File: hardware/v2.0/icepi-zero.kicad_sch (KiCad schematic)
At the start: 29 parts, among them J1 Conn_02x20_Counter_Clockwise, SW1 SW_Push, SW2 SW_Push, U1 ECP5U-25F-CABGA256, Y1 SG-8018CG 50.000000MHz

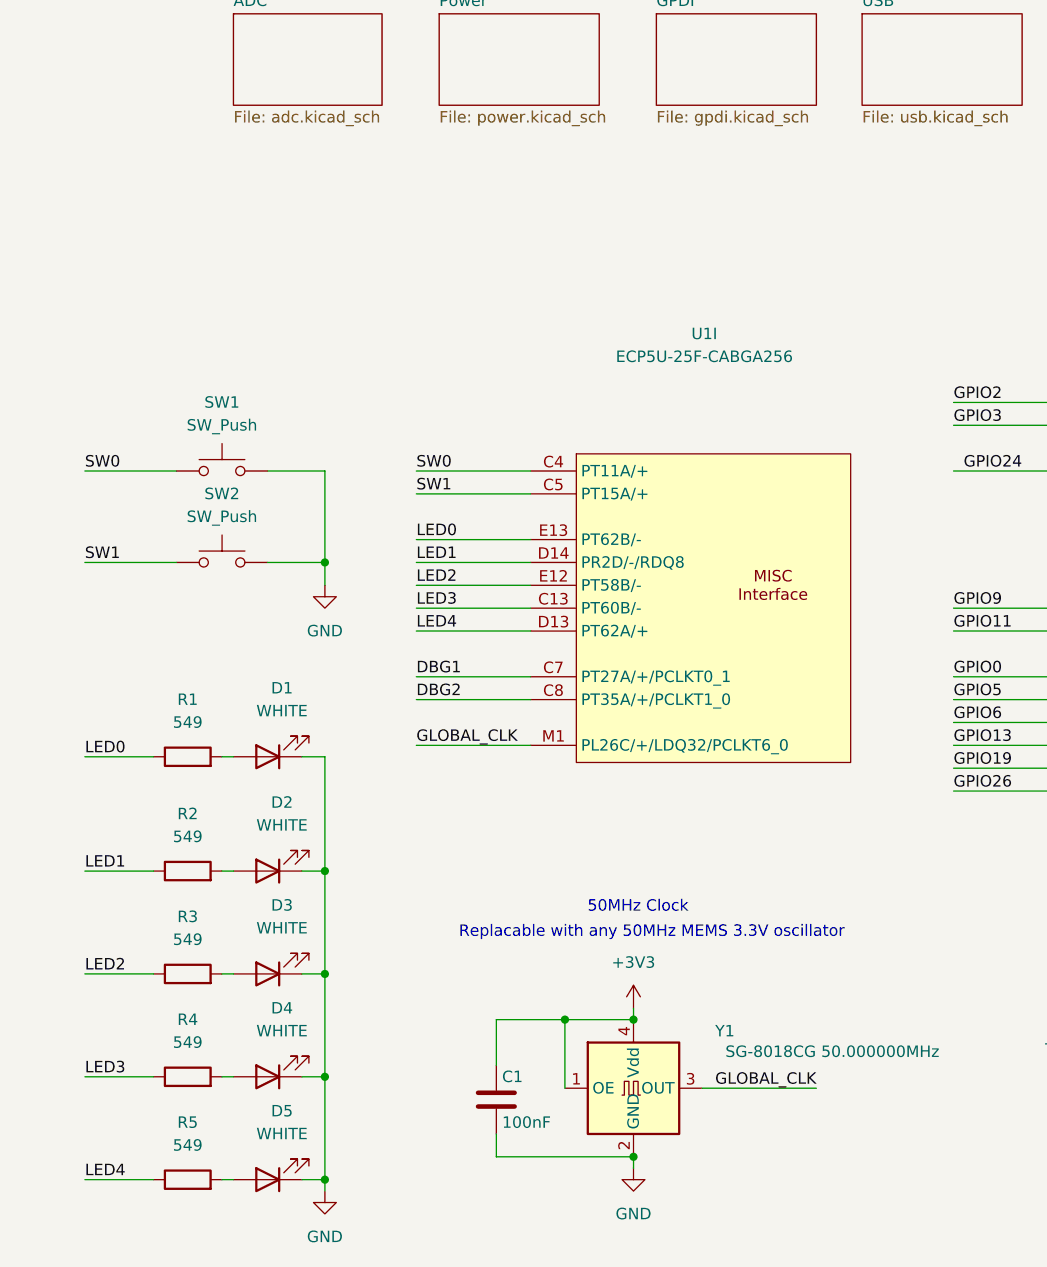
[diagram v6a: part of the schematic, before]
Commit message: LEDs update for IC
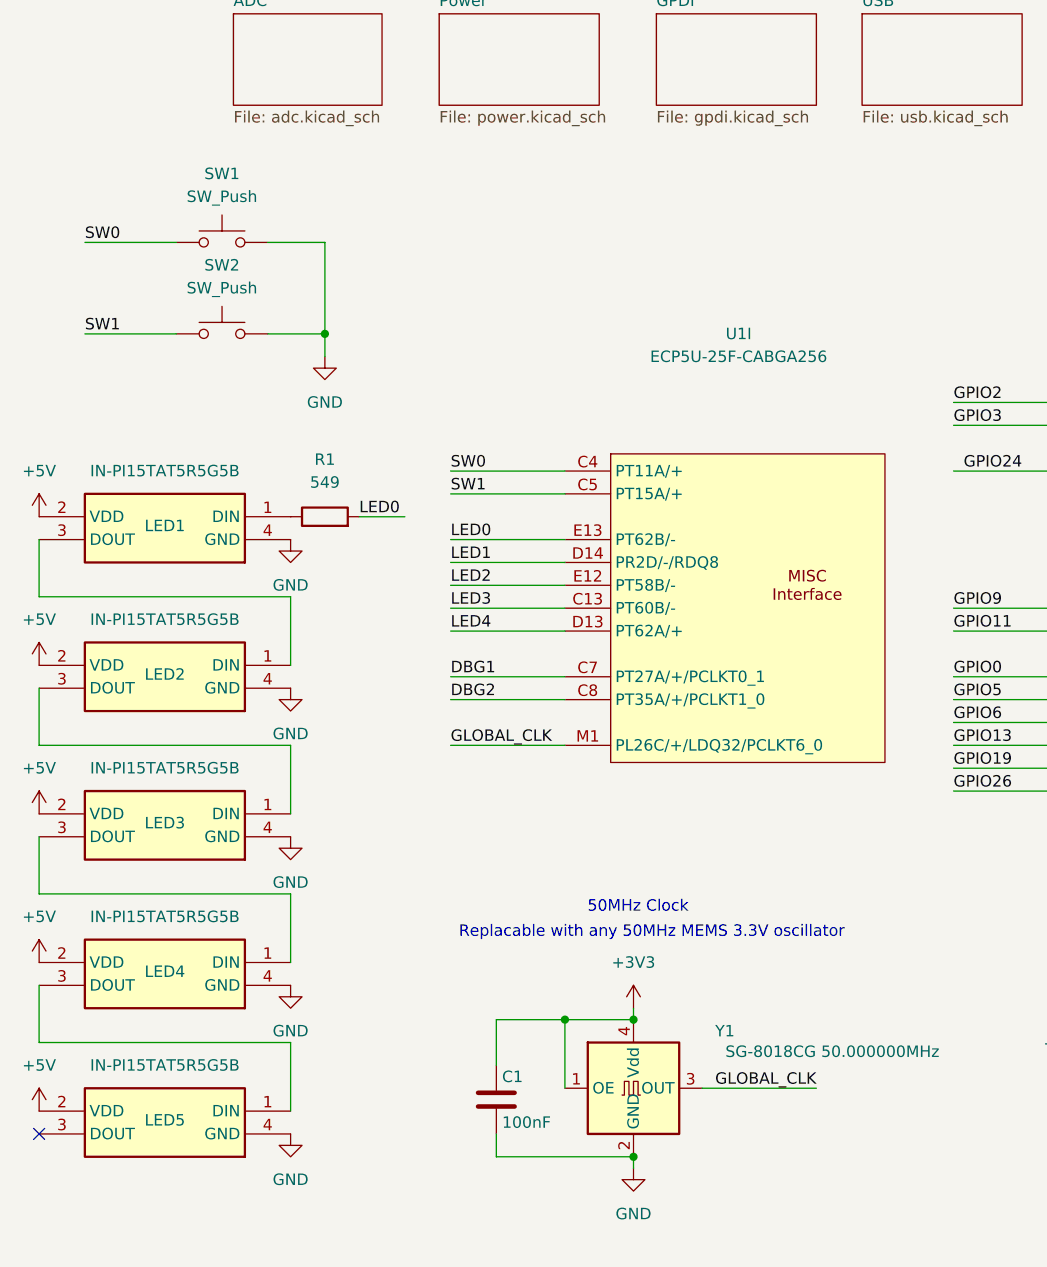
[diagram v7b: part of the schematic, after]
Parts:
- removed D1, D2, D3, D4, D5: WHITE, LED_SMD:LED_0603_1608Metric, symbol Device:LED
- removed R2, R3, R4, R5: 549, Resistor_SMD:R_0402_1005Metric, symbol Device:R
- added LED1, LED2, LED3, LED4, LED5: IN-PI15TAT5R5G5B, INPI15TAT5R5G5B, symbol IN-PI15TAT5R5G5B:IN-PI15TAT5R5G5B
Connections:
- net +5V: now also LED1.2 (VDD), LED2.2 (VDD), LED3.2 (VDD), LED4.2 (VDD), LED5.2 (VDD)
- net GND: now also LED1.4 (GND), LED2.4 (GND), LED3.4 (GND), LED4.4 (GND), LED5.4 (GND)
- net LED0: now also R1.2; no longer R1.1
- new net: LED1.1 (DIN), R1.1
- new net: LED2.3 (DOUT), LED3.1 (DIN)
- new net: LED3.3 (DOUT), LED4.1 (DIN)
- new net: LED1.3 (DOUT), LED2.1 (DIN)
- new net: LED4.3 (DOUT), LED5.1 (DIN)
- no-connect marks 5 -> 6
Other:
- moved on the sheet: R1, SW1, SW2, U1I

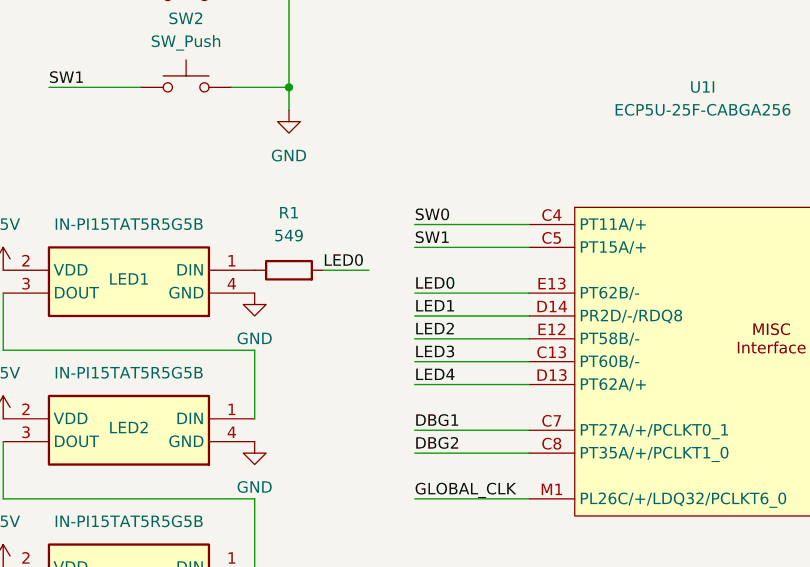
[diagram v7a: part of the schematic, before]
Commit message: ADC driver enable pin
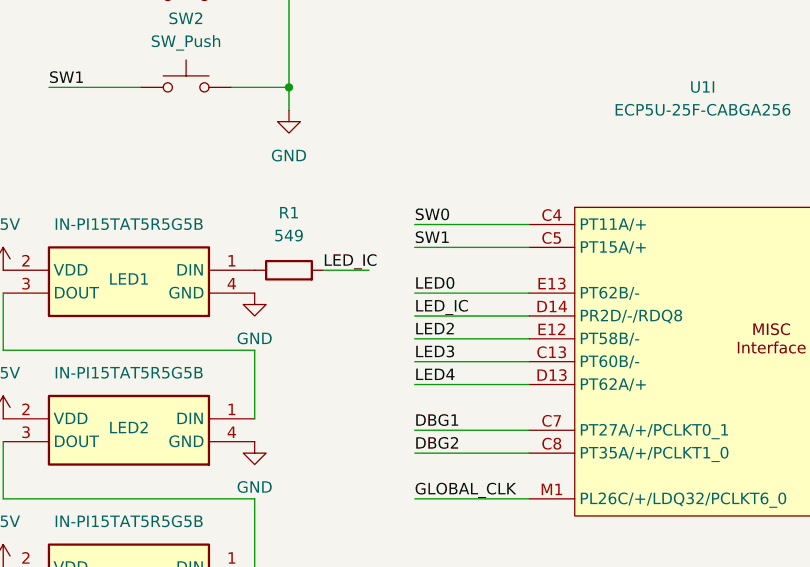
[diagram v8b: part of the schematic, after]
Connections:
- net LED0: no longer R1.2
- net LED1 renamed LED_IC
- net LED_IC: now also R1.2
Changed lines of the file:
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@@
 		)
 	)
-	(label "LED0"
+	(label "LED_IC"
 		(at 52.07 110.49 0)
 		(effects
@@
 		)
 	)
-	(label "LED1"
+	(label "LED_IC"
 		(at 62.23 115.57 0)
 		(effects
